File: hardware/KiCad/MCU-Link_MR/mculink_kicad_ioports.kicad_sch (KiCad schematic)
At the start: 8 parts, among them J3 Jumper_2_Open, J4 Jumper_2_Open, J5 Jumper_2_Open, SW1 KMR221GLFS, U1 LPC55S69JBD64

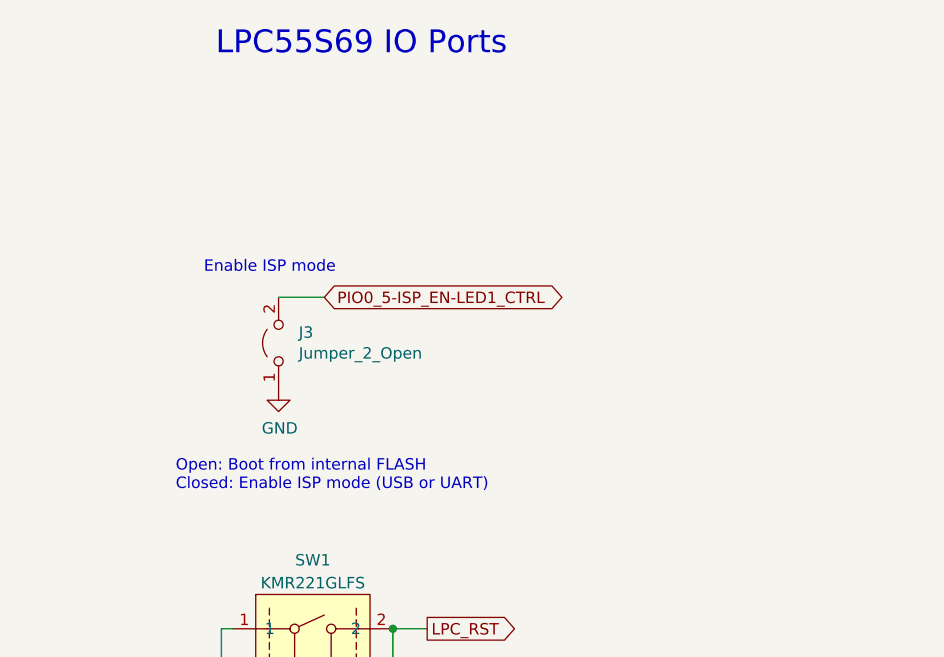
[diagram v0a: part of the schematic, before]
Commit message: sent v0.2 to PCB production
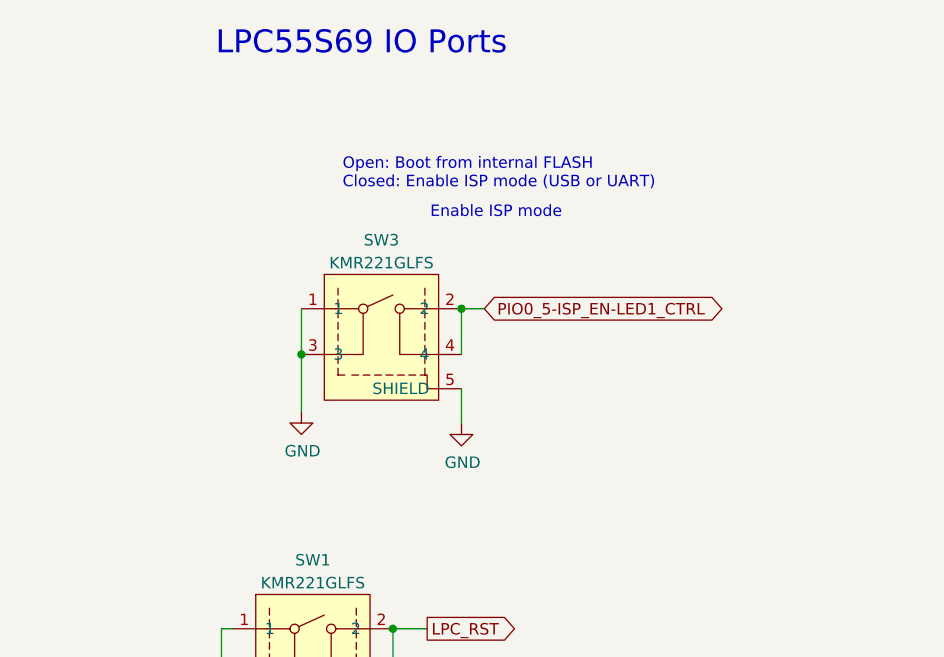
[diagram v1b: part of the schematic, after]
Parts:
- removed J3: Jumper_2_Open, Connector_PinHeader_2.54mm:PinHeader_1x02_P2.54mm_Vertical, symbol Jumper:Jumper_2_Open
- added SW3: KMR221GLFS, McuOnEclipse:SW_C_K_KMR2, symbol mculink_kicad:KMR221GLFS
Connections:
- net GND: now also SW3.1, SW3.3, SW3.5 (SHIELD)
- net PIO0_5-ISP_EN-LED1_CTRL: now also SW3.2, SW3.4
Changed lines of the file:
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@@
+	)
+	(junction
+		(at 138.43 57.15)
+		(diameter 0)
+		(color 0 0 0 0)
+	)
+	(junction
+		(at 156.21 52.07)
+		(diameter 0)
+		(color 0 0 0 0)
 	)
 	(junction
@@
 	(wire
 		(pts
+			(xy 156.21 60.96) (xy 156.21 64.77)
+		)
+		(stroke
+			(width 0)
+			(type default)
+		)
+	)
+	(wire
+		(pts
 			(xy 44.45 30.48) (xy 50.8 30.48)
 		)
@@
 	(wire
 		(pts
-			(xy 135.89 50.8) (xy 140.97 50.8)
-		)
-		(stroke
-			(width 0)
-			(type default)
-		)
-	)
-	(wire
-		(pts
 			(xy 232.41 143.51) (xy 232.41 149.86)
 		)
@@
 	(wire
 		(pts
+			(xy 138.43 52.07) (xy 138.43 57.15)
+		)
+		(stroke
+			(width 0)
+			(type default)
+		)
+	)
+	(wire
+		(pts
 			(xy 232.41 149.86) (xy 229.87 149.86)
 		)
@@
 	(wire
 		(pts
+			(xy 138.43 57.15) (xy 138.43 63.5)
+		)
+		(stroke
+			(width 0)
+			(type default)
+		)
+	)
+	(wire
+		(pts
 			(xy 172.72 125.73) (xy 181.61 125.73)
 		)
@@
 	(wire
 		(pts
+			(xy 156.21 52.07) (xy 158.75 52.07)
+		)
+		(stroke
+			(width 0)
+			(type default)
+		)
+	)
+	(wire
+		(pts
 			(xy 130.81 92.71) (xy 129.54 92.71)
 		)
@@
 		(pts
 			(xy 44.45 73.66) (xy 50.8 73.66)
+		)
+		(stroke
+			(width 0)
+			(type default)
+		)
+	)
+	(wire
+		(pts
+			(xy 156.21 52.07) (xy 156.21 57.15)
 		)
 		(stroke
@@
 	(text "Open: Boot from internal FLASH\nClosed: Enable ISP mode (USB or UART)"
 		(exclude_from_sim no)
-		(at 124.46 72.39 0)
+		(at 143.002 38.862 0)
 		(effects
 			(font
@@
 	(text "Enable ISP mode"
 		(exclude_from_sim no)
-		(at 142.24 48.26 0)
+		(at 167.386 42.164 0)
 		(effects
 			(font
@@
 	(global_label "PIO0_5-ISP_EN-LED1_CTRL"
 		(shape bidirectional)
-		(at 140.97 50.8 0)
+		(at 158.75 52.07 0)
 		(effects
 			(font
@@
 		)
 		(property "Intersheetrefs" "${INTERSHEET_REFS}"
-			(at 140.97 50.8 0)
+			(at 158.75 52.07 0)
 			(effects
 				(font
@@
 	)
 	(symbol
-		(lib_id "Jumper:Jumper_2_Open")
-		(at 135.89 55.88 90)
-		(unit 1)
-		(exclude_from_sim no)
-		(in_bom yes)
-		(on_board yes)
-		(dnp no)
-		(property "Reference" "J3"
-			(at 138.1252 54.7116 90)
-			(effects
-				(font
-					(size 1.27 1.27)
-				)
-				(justify right)
-			)
-		)
-		(property "Value" "Jumper_2_Open"
-			(at 138.1252 57.023 90)
-			(effects
-				(font
-					(size 1.27 1.27)
-				)
-				(justify right)
-			)
-		)
-		(property "Footprint" "Connector_PinHeader_2.54mm:PinHeader_1x02_P2.54mm_Vertical"
-			(at 135.89 55.88 0)
-			(effects
-				(font
-					(size 1.27 1.27)
-				)
-				(hide yes)
-			)
-		)
-		(property "Datasheet" "~"
-			(at 135.89 55.88 0)
-			(effects
-				(font
-					(size 1.27 1.27)
-				)
-				(hide yes)
-			)
-		)
-		(property "Description" "Jumper, 2-pole, open"
-			(at 135.89 55.88 0)
-			(effects
-				(font
-					(size 1.27 1.27)
-				)
-				(hide yes)
-			)
-		)
-		(property "distrelec#" ""
-			(at 135.89 55.88 0)
-			(effects
-				(font
-					(size 1.27 1.27)
-				)
-				(hide yes)
-			)
-		)
-		(pin "1"
-		)
-		(pin "2"
-		)
-		(instances
-			(project "MCU-Link_MR"
-				(path "/5d025764-753a-4b80-8d3d-c9a8a22c9527/00000000-0000-0000-0000-0000603cfdf2"
-					(reference "J3")
-					(unit 1)
-				)
-			)
-		)
-	)
-	(symbol
-		(lib_id "power:GND")
-		(at 135.89 60.96 0)
-		(unit 1)
-		(exclude_from_sim no)
-		(in_bom yes)
-		(on_board yes)
-		(dnp no)
-		(property "Reference" "#PWR039"
-			(at 135.89 67.31 0)
-			(effects
-				(font
-					(size 1.27 1.27)
-				)
-				(hide yes)
-			)
-		)
-		(property "Value" "GND"
-			(at 136.017 65.3542 0)
-			(effects
-				(font
-					(size 1.27 1.27)
-				)
-			)
-		)
-		(property "Footprint" ""
-			(at 135.89 60.96 0)
-			(effects
-				(font
-					(size 1.27 1.27)
-				)
-				(hide yes)
-			)
-		)
-		(property "Datasheet" ""
-			(at 135.89 60.96 0)
-			(effects
-				(font
-					(size 1.27 1.27)
-				)
-				(hide yes)
-			)
-		)
-		(property "Description" "Power symbol creates a global label with name \"GND\" , ground"
-			(at 135.89 60.96 0)
-			(effects
-				(font
-					(size 1.27 1.27)
-				)
-				(hide yes)
-			)
-		)
-		(pin "1"
-		)
-		(instances
-			(project "MCU-Link_MR"
-				(path "/5d025764-753a-4b80-8d3d-c9a8a22c9527/00000000-0000-0000-0000-0000603cfdf2"
-					(reference "#PWR039")
-					(unit 1)
-				)
-			)
-		)
-	)
-	(symbol
 		(lib_id "mculink_kicad:KMR221GLFS")
 		(at 139.7 92.71 0)
@@
 					(unit 1)
 				)
+			)
+		)
+	)
+	(symbol
+		(lib_id "power:GND")
+		(at 156.21 64.77 0)
+		(unit 1)
+		(exclude_from_sim no)
+		(in_bom yes)
+		(on_board yes)
+		(dnp no)
+		(property "Reference" "#PWR097"
+			(at 156.21 71.12 0)
+			(effects
+				(font
+					(size 1.27 1.27)
+				)
+				(hide yes)
+			)
+		)
+		(property "Value" "GND"
+			(at 156.337 69.1642 0)
+			(effects
+				(font
+					(size 1.27 1.27)
+				)
+			)
+		)
+		(property "Footprint" ""
+			(at 156.21 64.77 0)
+			(effects
+				(font
+					(size 1.27 1.27)
+				)
+				(hide yes)
+			)
+		)
+		(property "Datasheet" ""
+			(at 156.21 64.77 0)
+			(effects
+				(font
+					(size 1.27 1.27)
+				)
+				(hide yes)
+			)
+		)
+		(property "Description" "Power symbol creates a global label with name \"GND\" , ground"
+			(at 156.21 64.77 0)
+			(effects
+				(font
+					(size 1.27 1.27)
+				)
+				(hide yes)
+			)
+		)
+		(pin "1"
+		)
+		(instances
+			(project "MCU-Link_MR"
+				(path "/5d025764-753a-4b80-8d3d-c9a8a22c9527/00000000-0000-0000-0000-0000603cfdf2"
+					(reference "#PWR097")
+					(unit 1)
+				)
+			)
+		)
+	)
+	(symbol
+		(lib_id "power:GND")
+		(at 138.43 63.5 0)
+		(unit 1)
+		(exclude_from_sim no)
+		(in_bom yes)
+		(on_board yes)
+		(dnp no)
+		(property "Reference" "#PWR039"
+			(at 138.43 69.85 0)
+			(effects
+				(font
+					(size 1.27 1.27)
+				)
+				(hide yes)
+			)
+		)
+		(property "Value" "GND"
+			(at 138.557 67.8942 0)
+			(effects
+				(font
+					(size 1.27 1.27)
+				)
+			)
+		)
+		(property "Footprint" ""
+			(at 138.43 63.5 0)
+			(effects
+				(font
+					(size 1.27 1.27)
+				)
+				(hide yes)
+			)
+		)
+		(property "Datasheet" ""
+			(at 138.43 63.5 0)
+			(effects
+				(font
+					(size 1.27 1.27)
+				)
+				(hide yes)
+			)
+		)
+		(property "Description" "Power symbol creates a global label with name \"GND\" , ground"
+			(at 138.43 63.5 0)
+			(effects
+				(font
+					(size 1.27 1.27)
+				)
+				(hide yes)
+			)
+		)
+		(pin "1"
+		)
+		(instances
+			(project "MCU-Link_MR"
+				(path "/5d025764-753a-4b80-8d3d-c9a8a22c9527/00000000-0000-0000-0000-0000603cfdf2"
+					(reference "#PWR039")
+					(unit 1)
+				)
+			)
+		)
+	)
+	(symbol
+		(lib_id "mculink_kicad:KMR221GLFS")
+		(at 147.32 57.15 0)
+		(unit 1)
+		(exclude_from_sim no)
+		(in_bom yes)
+		(on_board yes)
+		(dnp no)
+		(property "Reference" "SW3"
+			(at 147.32 44.45 0)
+			(effects
+				(font
+					(size 1.27 1.27)
+				)
+			)
+		)
+		(property "Value" "KMR221GLFS"
+			(at 147.32 46.99 0)
+			(effects
+				(font
+					(size 1.27 1.27)
+				)
+			)
+		)
+		(property "Footprint" "McuOnEclipse:SW_C_K_KMR2"
+			(at 142.24 66.04 0)
+			(effects
+				(font
+					(size 1.27 1.27)
+				)
+				(hide yes)
+			)
+		)
+		(property "Datasheet" ""
+			(at 142.24 66.04 0)
+			(effects
+				(font
+					(size 1.27 1.27)
+				)
+				(hide yes)
+			)
+		)
+		(property "Description" ""
+			(at 147.32 57.15 0)
+			(effects
+				(font
+					(size 1.27 1.27)
+				)
+				(hide yes)
+			)
+		)
+		(property "distrelec#" ""
+			(at 147.32 57.15 0)
+			(effects
+				(font
+					(size 1.27 1.27)
+				)
+				(hide yes)
+			)
+		)
+		(pin "1"
+		)
+		(pin "2"
+		)
+		(pin "3"
+		)
+		(pin "4"
+		)
+		(pin "5"
+		)
+		(instances
+			(project "MCU-Link_MR"
+				(path "/5d025764-753a-4b80-8d3d-c9a8a22c9527/00000000-0000-0000-0000-0000603cfdf2"
+					(reference "SW3")
+					(unit 1)
+				)
